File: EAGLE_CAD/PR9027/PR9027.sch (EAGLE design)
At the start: 59 parts, among them SW1 C&K_PTS645, U1 SI4702-C19-GMR, X1 ABS25XTAL

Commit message: PEM Nuts & MFG#s
Updated PEM nut footprint OD to 6.6mm
Also updated the MFG part numbers on
- LED (HSMA-C265) AMBER!
- FET (AO3415A)
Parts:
- FET1: MFG_PN AO3435 -> AO3415A
- L1: MFG_PN AISC-0805-R18J-T -> AISC-0805-R18J-T
- LED: MFG_PN HSMC-C265 -> HSMA-C265
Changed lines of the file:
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@@
 <attribute name="CURRENT" value="400mA"/>
 <attribute name="DCR" value="640m"/>
-<attribute name="MFG_PN" value="AISC-0805-R18J-T"/>
+<attribute name="MFG_PN" value="AISC-0805-R18J-T
+"/>
 <attribute name="TOL" value="5%"/>
 </part>
@@
 </part>
 <part name="FET1" library="PR_Parts_Library" deviceset="AO3435" device="" value="">
-<attribute name="MFG_PN" value="AO3435"/>
+<attribute name="MFG_PN" value="AO3415A"/>
 </part>
 <part name="SPKR_PLACE" library="PR_Parts_Library" deviceset="PR2024_SPKR_SMD" device="" value="PR2024_SPKR_SMD"/>
@@
 </part>
 <part name="LED" library="PR_Parts_Library" deviceset="HSMC-C265_REVERSE_MOUNT_LED" device="">
-<attribute name="MFG_PN" value="HSMC-C265"/>
+<attribute name="MFG_PN" value="HSMA-C265"/>
 </part>
 <part name="U$2" library="PR_Parts_Library" deviceset="PEM_SMT" device=""/>

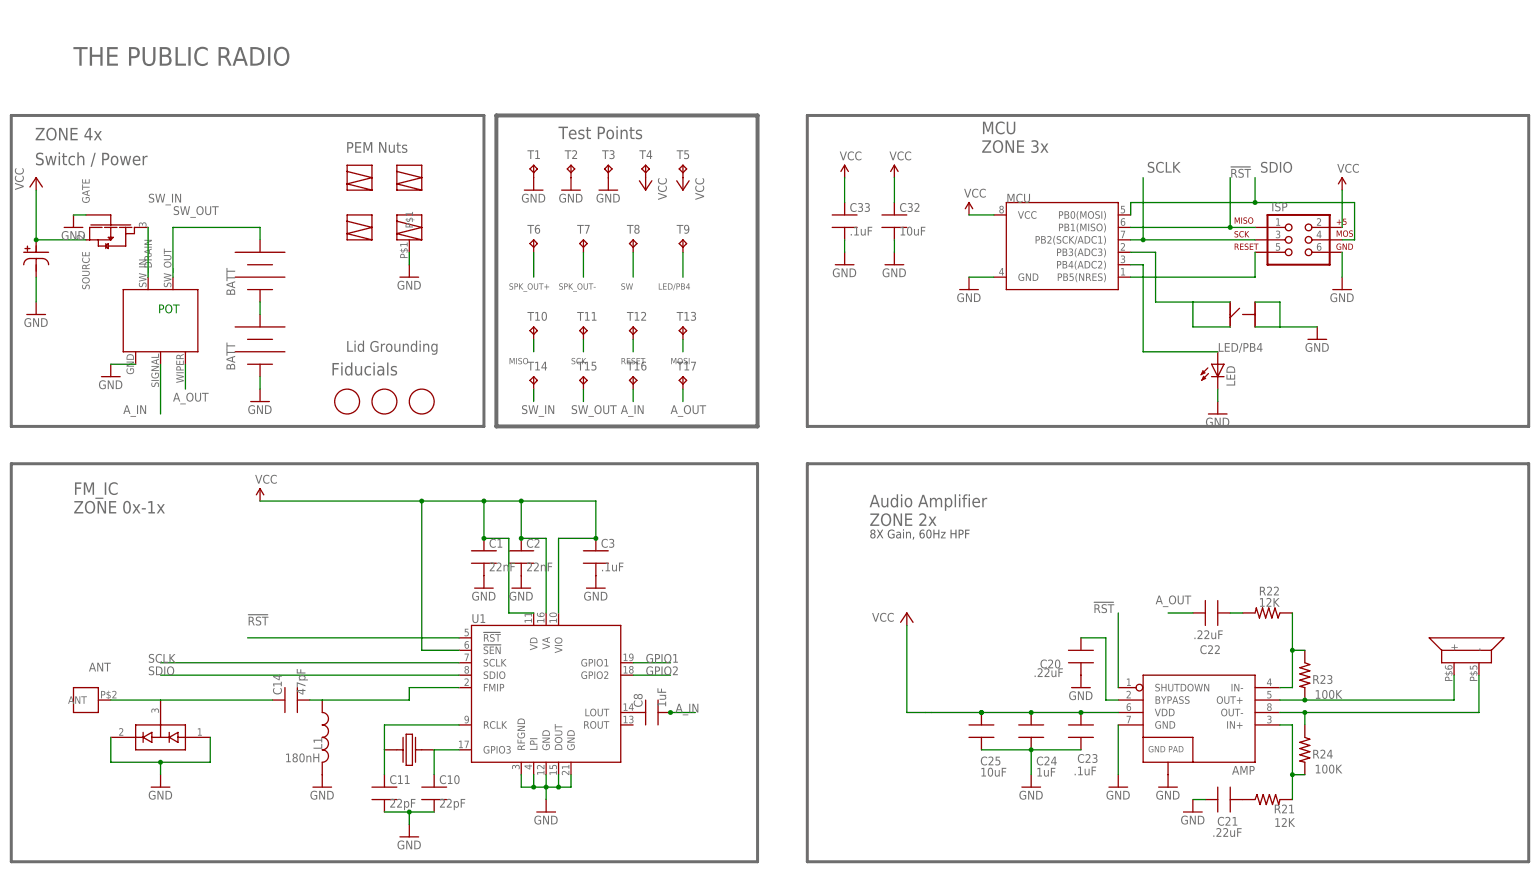
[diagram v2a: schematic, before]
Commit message: updated for production
archived 9026. cleaned up the speaker and pem nut stuff in the libary. made the speaker cutout as big as possible.
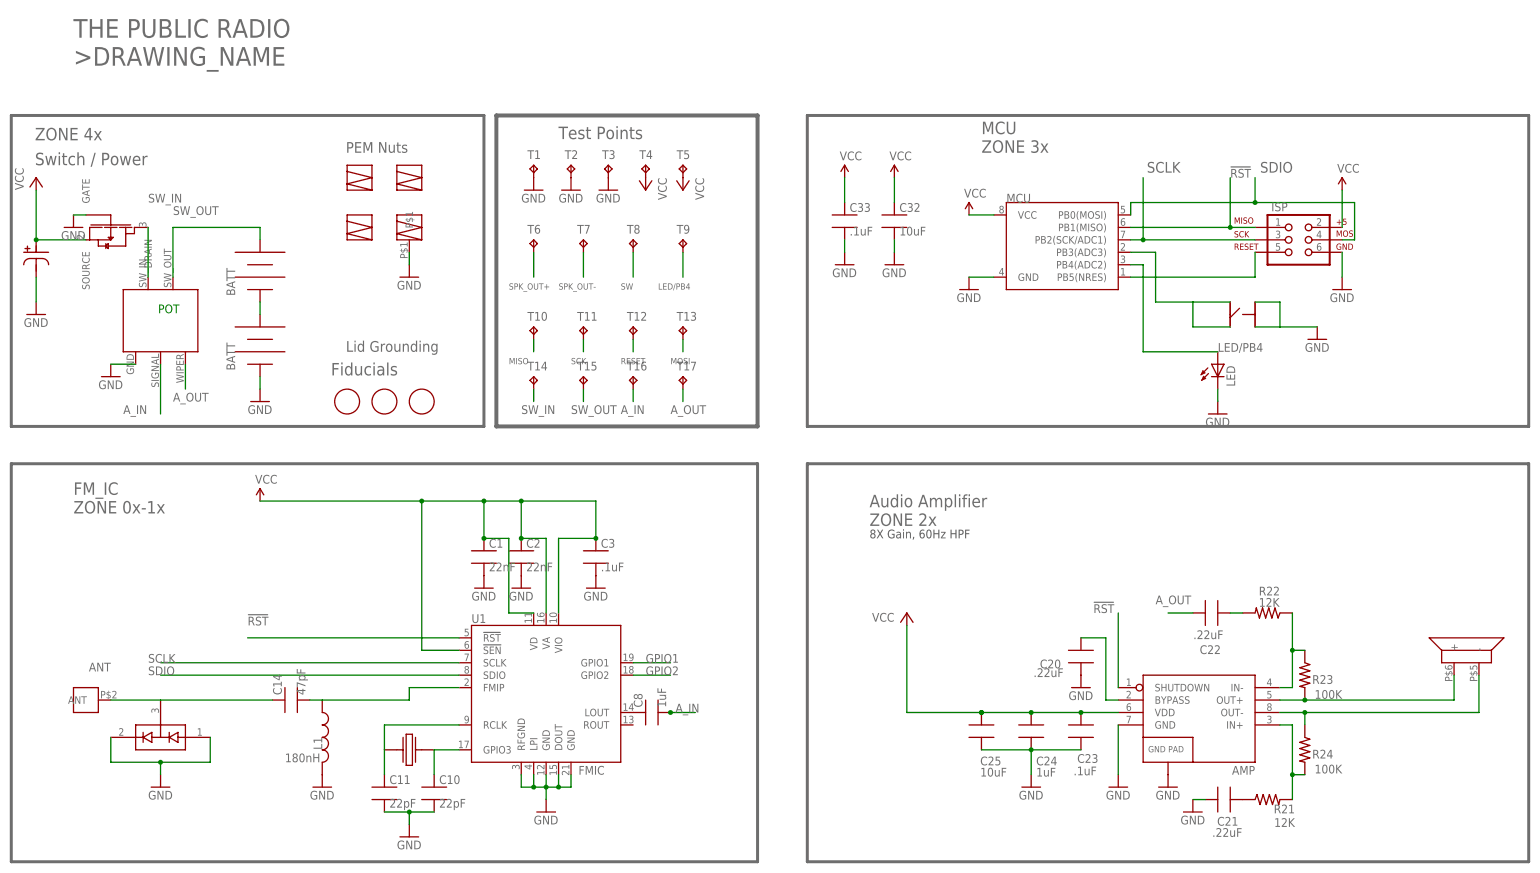
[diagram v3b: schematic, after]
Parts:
- removed SPKR_PLACE: PR2024_SPKR_SMD, PR_Parts_Library:PR2024_SPKR_SMD
- removed U$2, U$3, U$4: PEM_SMT, PR_Parts_Library:PEM_SMT
- removed U$5: PEM_M3_SMT_W/PIN, PR_Parts_Library:PEM_M3_SMT_W/PIN
- added SPEAKER: PR2023_GROUND_UP_SPEAKER, PR_Parts_Library:PR2023_GROUND_UP_SPEAKER
- added SPEAKER_PEM_1, SPEAKER_PEM_2, SPEAKER_PEM_4: PEM_M3_ONE_SIDE, PR_Parts_Library:PEM_M3_ONE_SIDE
- added SPEAKER_PEM_3: PEM_M3_ONE_SIDE_W/PIN, PR_Parts_Library:PEM_M3_ONE_SIDE_W/PIN
- ANT_MOUNT: value DNP -> PEM_M3; device PR_Parts_Library:M3_PEMNUT -> PR_Parts_Library:PEM_M3
- T1, T10, T11, T12, T13, T14, T15, T16, T17, T2, T3, T4, T5, T6, T7, T8, T9: value (none) -> TPTP20R
- U1: value SI4702-C19-GMR -> FMIC
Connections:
- net GND: now also SPEAKER_PEM_3.P$1; no longer U$5.P$1
- net SPK_OUT+: now also SPEAKER.+; no longer SPKR_PLACE.+
- net SPK_OUT-: now also SPEAKER.-; no longer SPKR_PLACE.-
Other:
- note added: "THE PUBLIC RADIO >DRAWING_NAME"
- note removed: "THE PUBLIC RADIO"
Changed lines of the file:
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@@
 <?xml version="1.0" encoding="utf-8"?>
 <!DOCTYPE eagle SYSTEM "eagle.dtd">
-<eagle version="6.6.0">
+<eagle version="7.7.0">
 <drawing>
 <settings>
@@
 <setting verticaltext="up"/>
 </settings>
-<grid distance="0.1" unitdist="inch" unit="inch" style="lines" multiple="1" display="no" altdistance="0.01" altunitdist="inch" altunit="inch"/>
+<grid distance="0.5" unitdist="mm" unit="mm" style="dots" multiple="1" display="no" altdistance="0.1" altunitdist="mm" altunit="mm"/>
 <layers>
 <layer number="1" name="Top" color="4" fill="1" visible="no" active="no"/>
@@
 </classes>
 <parts>
-<part name="U1" library="PR_Parts_Library" deviceset="SI4702-C19-GMR" device="" value="">
+<part name="U1" library="PR_Parts_Library" deviceset="SI4702-C19-GMR" device="" value="FMIC">
 <attribute name="MFG_PN" value="Si4702 C19 GM - supplied by CL Labs"/>
 </part>
@@
 <part name="GND24" library="SparkFun-Aesthetics" deviceset="GND" device=""/>
 <part name="P+1" library="supply1" deviceset="VCC" device=""/>
-<part name="ANT_MOUNT" library="PR_Parts_Library" deviceset="M3_PEMNUT" device="" value="DNP"/>
+<part name="ANT_MOUNT" library="PR_Parts_Library" deviceset="PEM_M3" device="" value="PEM_M3"/>
 <part name="R1" library="PR_Parts_Library" deviceset="VOLUME_POT" device="" value="VOLUME_POT"/>
 <part name="GND5" library="SparkFun-Aesthetics" deviceset="GND" device=""/>
@@
 <attribute name="CURRENT" value="400mA"/>
 <attribute name="DCR" value="640m"/>
-<attribute name="MFG_PN" value="AISC-0805-R18J-T
-"/>
+<attribute name="MFG_PN" value="AISC-0805-R18J-T "/>
 <attribute name="TOL" value="5%"/>
 </part>
@@
 <attribute name="MFG_PN" value="AO3415A"/>
 </part>
-<part name="SPKR_PLACE" library="PR_Parts_Library" deviceset="PR2024_SPKR_SMD" device="" value="PR2024_SPKR_SMD"/>
+<part name="SPEAKER" library="PR_Parts_Library" deviceset="PR2023_GROUND_UP_SPEAKER" device="" value="PR2023_GROUND_UP_SPEAKER"/>
 <part name="T14" library="PR_Parts_Library" deviceset="TP" device="TP20R"/>
 <part name="T15" library="PR_Parts_Library" deviceset="TP" device="TP20R"/>
@@
 <attribute name="MFG_PN" value="HSMA-C265"/>
 </part>
-<part name="U$2" library="PR_Parts_Library" deviceset="PEM_SMT" device=""/>
-<part name="U$3" library="PR_Parts_Library" deviceset="PEM_SMT" device=""/>
-<part name="U$4" library="PR_Parts_Library" deviceset="PEM_SMT" device=""/>
-<part name="U$5" library="PR_Parts_Library" deviceset="PEM_M3_SMT_W/PIN" device=""/>
+<part name="SPEAKER_PEM_1" library="PR_Parts_Library" deviceset="PEM_M3_ONE_SIDE" device=""/>
+<part name="SPEAKER_PEM_2" library="PR_Parts_Library" deviceset="PEM_M3_ONE_SIDE" device=""/>
+<part name="SPEAKER_PEM_4" library="PR_Parts_Library" deviceset="PEM_M3_ONE_SIDE" device=""/>
+<part name="SPEAKER_PEM_3" library="PR_Parts_Library" deviceset="PEM_M3_ONE_SIDE_W/PIN" device=""/>
 </parts>
 <sheets>
@@
 <text x="157.48" y="144.78" size="2.54" layer="96">MCU
 ZONE 3x</text>
-<text x="-27.94" y="162.56" size="3.81" layer="96">THE PUBLIC RADIO</text>
+<text x="-27.94" y="162.56" size="3.81" layer="96">THE PUBLIC RADIO
+&gt;DRAWING_NAME</text>
 <text x="24.638" y="99.314" size="2.54" layer="96">Fiducials </text>
 <text x="71.12" y="147.574" size="2.54" layer="96">Test Points </text>
@@
 <instance part="C8" gate="G$1" x="88.9" y="30.48" rot="R90"/>
 <instance part="FET1" gate="G$1" x="-20.32" y="129.54" rot="R270"/>
-<instance part="SPKR_PLACE" gate="G$1" x="256.54" y="40.64" rot="R90"/>
+<instance part="SPEAKER" gate="G$1" x="256.54" y="40.64" rot="R90"/>
 <instance part="T14" gate="G$1" x="66.04" y="99.06"/>
 <instance part="T15" gate="G$1" x="76.2" y="99.06"/>
@@
 <attribute name="MFG_PN" x="205.74" y="101.6" size="1.778" layer="96" display="off"/>
 </instance>
-<instance part="U$2" gate="G$1" x="30.48" y="139.7"/>
-<instance part="U$3" gate="G$1" x="40.64" y="139.7"/>
-<instance part="U$4" gate="G$1" x="30.48" y="129.54"/>
-<instance part="U$5" gate="G$1" x="40.64" y="129.54"/>
+<instance part="SPEAKER_PEM_1" gate="G$1" x="30.48" y="139.7"/>
+<instance part="SPEAKER_PEM_2" gate="G$1" x="40.64" y="139.7"/>
+<instance part="SPEAKER_PEM_4" gate="G$1" x="30.48" y="129.54"/>
+<instance part="SPEAKER_PEM_3" gate="G$1" x="40.64" y="129.54"/>
 </instances>
 <busses>
@@
 </segment>
 <segment>
-<pinref part="U$5" gate="G$1" pin="P$1"/>
+<pinref part="SPEAKER_PEM_3" gate="G$1" pin="P$1"/>
 <wire x1="40.64" y1="121.92" x2="40.64" y2="124.46" width="0.1524" layer="91"/>
 <pinref part="GND12" gate="1" pin="GND"/>
@@
 </segment>
 <segment>
-<pinref part="SPKR_PLACE" gate="G$1" pin="+"/>
+<pinref part="SPEAKER" gate="G$1" pin="+"/>
 <wire x1="254" y1="33.02" x2="254" y2="38.1" width="0.1524" layer="91"/>
 <pinref part="AMP" gate="G$1" pin="OUT+"/>
@@
 </segment>
 <segment>
-<pinref part="SPKR_PLACE" gate="G$1" pin="-"/>
+<pinref part="SPEAKER" gate="G$1" pin="-"/>
 <wire x1="259.08" y1="30.48" x2="259.08" y2="38.1" width="0.1524" layer="91"/>
 <pinref part="AMP" gate="G$1" pin="OUT-"/>

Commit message: Part numbers and attributes
Cleaning up part attributes for slightly easier BOM exporting
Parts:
- ANT_MOUNT, SPEAKER_PEM_1, SPEAKER_PEM_2, SPEAKER_PEM_3, SPEAKER_PEM_4: CENTERLINE_PN (none) -> PR2040; MFG_PN (none) -> Consigned
- FET1: ALTERNATE_MFG_PN (none) -> AO3415A; MFG_PN AO3415A -> AO3435
- ISP: MFG_PN (none) -> DNP
- JP5, JP6: CENTERLINE_PN (none) -> PR2003; MFG_PN 2 of BK92 - supplied by CL Labs -> Consigned
- L1: ALTERNATE_MFG_PN (none) -> AISC-0805-R18G-T
- MCU: MFG_PN (none) -> ATTINY25-20SUR
- R1: CENTERLINE_PN (none) -> PR2030; MFG_PN (none) -> Consigned
- SPEAKER: CENTERLINE_PN (none) -> PR2033; MFG_PN (none) -> Consigned
- U1: MFG_PN Si4702 C19 GM - supplied by CL Labs -> SI4702-C19-GMR
